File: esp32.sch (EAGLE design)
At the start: 12 parts, among them IC1 LM1117IMPX-3.3, U1 ESP32MOD

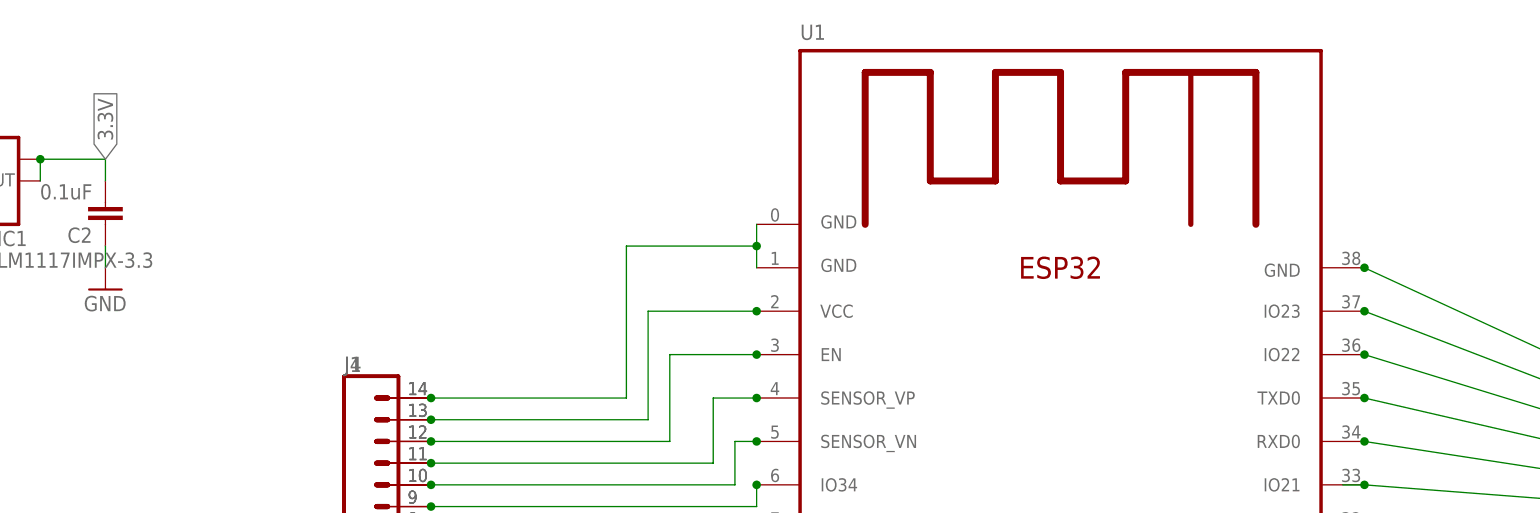
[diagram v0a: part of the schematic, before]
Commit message: Added the reset circuitry
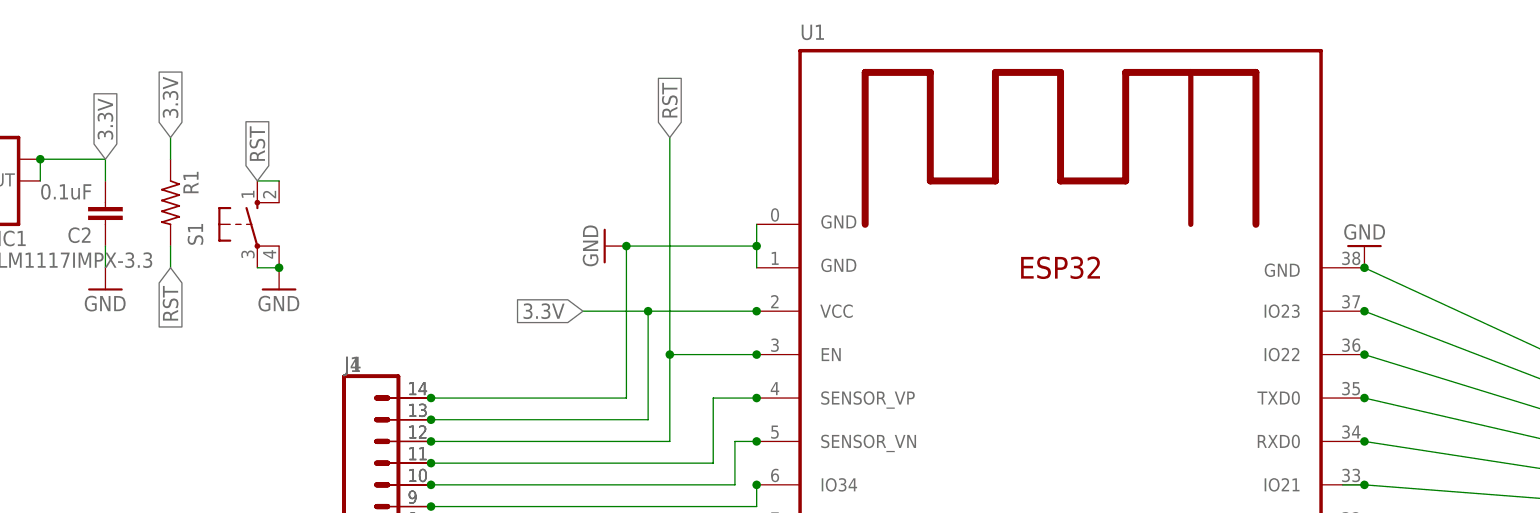
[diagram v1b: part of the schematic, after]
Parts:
- added R1: (no value), rcl:R-US_0411/15
- added S1: (no value), switch-omron:10-XX
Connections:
- removed net N$4: J1.13, J4.13, U1.VCC
- removed net N$5: J1.12, J4.12, U1.EN
- new net RST: J1.12, J4.12, R1.2, S1.S, S1.S1, U1.EN
- net 3.3V: now also J1.13, J4.13, R1.1, U1.VCC
- net GND: now also S1.P, S1.P1
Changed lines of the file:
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@@
 <grid distance="0.1" unitdist="inch" unit="inch" style="lines" multiple="1" display="no" altdistance="0.01" altunitdist="inch" altunit="inch"/>
 <layers>
-<layer number="1" name="Top" color="4" fill="1" visible="no" active="no"/>
-<layer number="16" name="Bottom" color="1" fill="1" visible="no" active="no"/>
-<layer number="17" name="Pads" color="2" fill="1" visible="no" active="no"/>
-<layer number="18" name="Vias" color="2" fill="1" visible="no" active="no"/>
-<layer number="19" name="Unrouted" color="6" fill="1" visible="no" active="no"/>
-<layer number="20" name="Dimension" color="15" fill="1" visible="no" active="no"/>
-<layer number="21" name="tPlace" color="7" fill="1" visible="no" active="no"/>
-<layer number="22" name="bPlace" color="7" fill="1" visible="no" active="no"/>
-<layer number="23" name="tOrigins" color="15" fill="1" visible="no" active="no"/>
-<layer number="24" name="bOrigins" color="15" fill="1" visible="no" active="no"/>
-<layer number="25" name="tNames" color="7" fill="1" visible="no" active="no"/>
-<layer number="26" name="bNames" color="7" fill="1" visible="no" active="no"/>
-<layer number="27" name="tValues" color="7" fill="1" visible="no" active="no"/>
-<layer number="28" name="bValues" color="7" fill="1" visible="no" active="no"/>
+<layer number="1" name="Top" color="4" fill="1" visible="yes" active="no"/>
+<layer number="16" name="Bottom" color="1" fill="1" visible="yes" active="no"/>
+<layer number="17" name="Pads" color="2" fill="1" visible="yes" active="no"/>
+<layer number="18" name="Vias" color="2" fill="1" visible="yes" active="no"/>
+<layer number="19" name="Unrouted" color="6" fill="1" visible="yes" active="no"/>
+<layer number="20" name="Dimension" color="15" fill="1" visible="yes" active="no"/>
+<layer number="21" name="tPlace" color="7" fill="1" visible="yes" active="no"/>
+<layer number="22" name="bPlace" color="7" fill="1" visible="yes" active="no"/>
+<layer number="23" name="tOrigins" color="15" fill="1" visible="yes" active="no"/>
+<layer number="24" name="bOrigins" color="15" fill="1" visible="yes" active="no"/>
+<layer number="25" name="tNames" color="7" fill="1" visible="yes" active="no"/>
+<layer number="26" name="bNames" color="7" fill="1" visible="yes" active="no"/>
+<layer number="27" name="tValues" color="7" fill="1" visible="yes" active="no"/>
+<layer number="28" name="bValues" color="7" fill="1" visible="yes" active="no"/>
 <layer number="29" name="tStop" color="7" fill="3" visible="no" active="no"/>
 <layer number="30" name="bStop" color="7" fill="6" visible="no" active="no"/>
@@
 <layer number="35" name="tGlue" color="7" fill="4" visible="no" active="no"/>
 <layer number="36" name="bGlue" color="7" fill="5" visible="no" active="no"/>
-<layer number="37" name="tTest" color="7" fill="1" visible="no" active="no"/>
-<layer number="38" name="bTest" color="7" fill="1" visible="no" active="no"/>
+<layer number="37" name="tTest" color="7" fill="1" visible="yes" active="no"/>
+<layer number="38" name="bTest" color="7" fill="1" visible="yes" active="no"/>
 <layer number="39" name="tKeepout" color="4" fill="11" visible="no" active="no"/>
 <layer number="40" name="bKeepout" color="1" fill="11" visible="no" active="no"/>
@@
 <layer number="44" name="Drills" color="7" fill="1" visible="no" active="no"/>
 <layer number="45" name="Holes" color="7" fill="1" visible="no" active="no"/>
-<layer number="46" name="Milling" color="3" fill="1" visible="no" active="no"/>
-<layer number="47" name="Measures" color="7" fill="1" visible="no" active="no"/>
-<layer number="48" name="Document" color="7" fill="1" visible="no" active="no"/>
-<layer number="49" name="Reference" color="7" fill="1" visible="no" active="no"/>
-<layer number="50" name="dxf" color="7" fill="1" visible="no" active="no"/>
-<layer number="51" name="tDocu" color="7" fill="1" visible="no" active="no"/>
-<layer number="52" name="bDocu" color="7" fill="1" visible="no" active="no"/>
-<layer number="53" name="tGND_GNDA" color="7" fill="9" visible="no" active="no"/>
-<layer number="54" name="bGND_GNDA" color="1" fill="9" visible="no" active="no"/>
-<layer number="56" name="wert" color="7" fill="1" visible="no" active="no"/>
-<layer number="57" name="tCAD" color="7" fill="1" visible="no" active="no"/>
-<layer number="59" name="tCarbon" color="7" fill="1" visible="no" active="no"/>
-<layer number="60" name="bCarbon" color="7" fill="1" visible="no" active="no"/>
+<layer number="46" name="Milling" color="3" fill="1" visible="yes" active="no"/>
+<layer number="47" name="Measures" color="7" fill="1" visible="yes" active="no"/>
+<layer number="48" name="Document" color="7" fill="1" visible="yes" active="no"/>
+<layer number="49" name="Reference" color="7" fill="1" visible="yes" active="no"/>
+<layer number="50" name="dxf" color="7" fill="1" visible="yes" active="no"/>
+<layer number="51" name="tDocu" color="7" fill="1" visible="yes" active="no"/>
+<layer number="52" name="bDocu" color="7" fill="1" visible="yes" active="no"/>
+<layer number="53" name="tGND_GNDA" color="7" fill="9" visible="yes" active="no"/>
+<layer number="54" name="bGND_GNDA" color="1" fill="9" visible="yes" active="no"/>
+<layer number="56" name="wert" color="7" fill="1" visible="yes" active="no"/>
+<layer number="57" name="tCAD" color="7" fill="1" visible="yes" active="no"/>
+<layer number="59" name="tCarbon" color="7" fill="1" visible="yes" active="no"/>
+<layer number="60" name="bCarbon" color="7" fill="1" visible="yes" active="no"/>
 <layer number="90" name="Modules" color="5" fill="1" visible="yes" active="yes"/>
 <layer number="91" name="Nets" color="2" fill="1" visible="yes" active="yes"/>
@@
 <part name="GND5" library="supply1" deviceset="GND" device=""/>
 <part name="J8" library="SparkFun-Connectors" deviceset="CONN_03" device=""/>
+<part name="R1" library="rcl" deviceset="R-US_" device="0411/15"/>
+<part name="S1" library="switch-omron" deviceset="10-XX" device=""/>
+<part name="GND6" library="supply1" deviceset="GND" device=""/>
+<part name="GND7" library="supply1" deviceset="GND" device=""/>
+<part name="GND8" library="supply1" deviceset="GND" device=""/>
 </parts>
 <sheets>
@@
 <instance part="GND5" gate="1" x="-71.12" y="68.58"/>
 <instance part="J8" gate="J$1" x="-91.44" y="48.26"/>
+<instance part="R1" gate="G$1" x="-38.1" y="78.74" rot="R270"/>
+<instance part="S1" gate="1" x="-27.94" y="76.2"/>
+<instance part="GND6" gate="1" x="-25.4" y="68.58"/>
+<instance part="GND7" gate="1" x="12.7" y="73.66" rot="R270"/>
+<instance part="GND8" gate="1" x="101.6" y="73.66" rot="R180"/>
 </instances>
 <busses>
@@
 <pinref part="J4" gate="G$1" pin="14"/>
 <junction x="-7.62" y="55.88"/>
+<pinref part="GND7" gate="1" pin="GND"/>
+<junction x="15.24" y="73.66"/>
 </segment>
 <segment>
@@
 <pinref part="J5" gate="G$1" pin="1"/>
 <junction x="134.62" y="55.88"/>
+<pinref part="GND8" gate="1" pin="GND"/>
 </segment>
 <segment>
@@
 <label x="-71.12" y="45.72" size="1.778" layer="95" rot="R90" xref="yes"/>
 </segment>
-</net>
-<net name="N$4" class="0">
-<segment>
-<pinref part="J1" gate="G$1" pin="13"/>
-<wire x1="-7.62" y1="53.34" x2="17.78" y2="53.34" width="0.1524" layer="91"/>
-<wire x1="17.78" y1="53.34" x2="17.78" y2="66.04" width="0.1524" layer="91"/>
-<pinref part="U1" gate="G$1" pin="VCC"/>
-<wire x1="17.78" y1="66.04" x2="30.48" y2="66.04" width="0.1524" layer="91"/>
-<junction x="30.48" y="66.04"/>
-<pinref part="J4" gate="G$1" pin="13"/>
-<junction x="-7.62" y="53.34"/>
-</segment>
-</net>
-<net name="N$5" class="0">
+<segment>
+<pinref part="S1" gate="1" pin="P"/>
+<pinref part="S1" gate="1" pin="P1"/>
+<wire x1="-27.94" y1="71.12" x2="-25.4" y2="71.12" width="0.1524" layer="91"/>
+<pinref part="GND6" gate="1" pin="GND"/>
+<junction x="-25.4" y="71.12"/>
+</segment>
+</net>
+<net name="RST" class="0">
 <segment>
 <pinref part="J1" gate="G$1" pin="12"/>
@@
 <pinref part="J4" gate="G$1" pin="12"/>
 <junction x="-7.62" y="50.8"/>
+<label x="20.32" y="86.36" size="1.778" layer="95" rot="R90" xref="yes"/>
+<wire x1="20.32" y1="60.96" x2="20.32" y2="86.36" width="0.1524" layer="91"/>
+<junction x="20.32" y="60.96"/>
+</segment>
+<segment>
+<pinref part="R1" gate="G$1" pin="2"/>
+<wire x1="-38.1" y1="73.66" x2="-38.1" y2="71.12" width="0.1524" layer="91"/>
+<label x="-38.1" y="71.12" size="1.778" layer="95" rot="R270" xref="yes"/>
+</segment>
+<segment>
+<pinref part="S1" gate="1" pin="S"/>
+<pinref part="S1" gate="1" pin="S1"/>
+<wire x1="-27.94" y1="81.28" x2="-25.4" y2="81.28" width="0.1524" layer="91"/>
+<label x="-27.94" y="81.28" size="1.778" layer="95" rot="R90" xref="yes"/>
 </segment>
 </net>
@@
 <label x="-76.2" y="48.26" size="1.778" layer="95" rot="R90" xref="yes"/>
 </segment>
+<segment>
+<pinref part="R1" gate="G$1" pin="1"/>
+<wire x1="-38.1" y1="83.82" x2="-38.1" y2="86.36" width="0.1524" layer="91"/>
+<label x="-38.1" y="86.36" size="1.778" layer="95" rot="R90" xref="yes"/>
+</segment>
+<segment>
+<pinref part="J1" gate="G$1" pin="13"/>
+<wire x1="-7.62" y1="53.34" x2="17.78" y2="53.34" width="0.1524" layer="91"/>
+<wire x1="17.78" y1="53.34" x2="17.78" y2="66.04" width="0.1524" layer="91"/>
+<pinref part="U1" gate="G$1" pin="VCC"/>
+<wire x1="17.78" y1="66.04" x2="30.48" y2="66.04" width="0.1524" layer="91"/>
+<junction x="30.48" y="66.04"/>
+<pinref part="J4" gate="G$1" pin="13"/>
+<junction x="-7.62" y="53.34"/>
+<label x="10.16" y="66.04" size="1.778" layer="95" rot="R180" xref="yes"/>
+<wire x1="10.16" y1="66.04" x2="17.78" y2="66.04" width="0.1524" layer="91"/>
+<junction x="17.78" y="66.04"/>
+</segment>
+</net>
+<net name="GND1" class="0">
 </net>
 </nets>

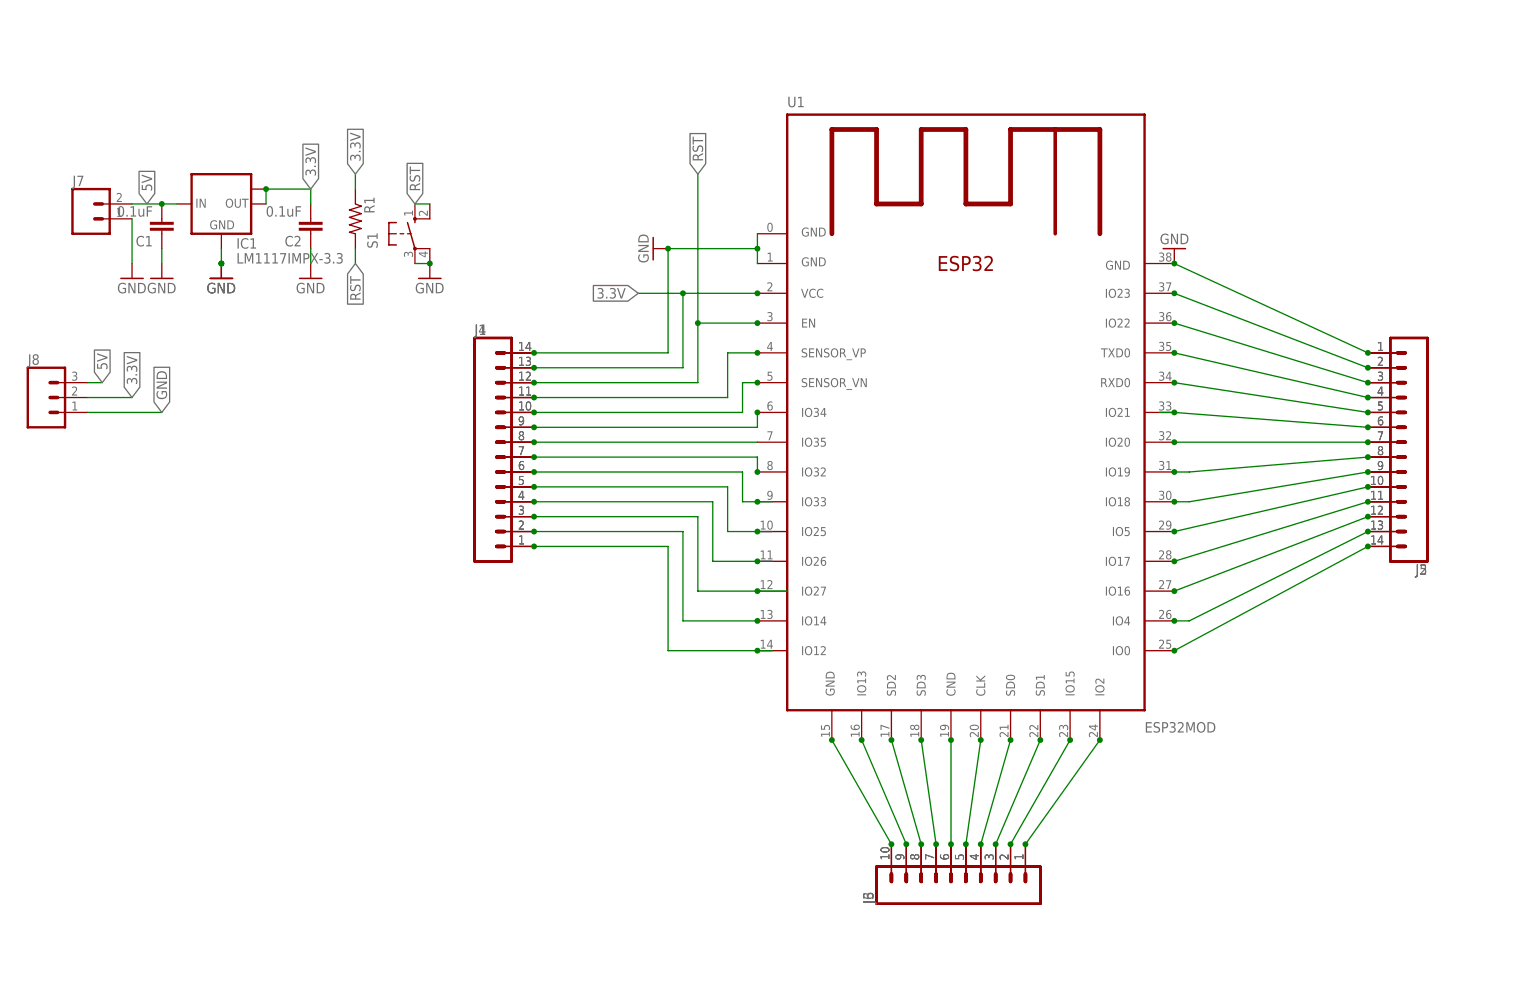
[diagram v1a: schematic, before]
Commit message: Added all the GPIO strapping bias resistors
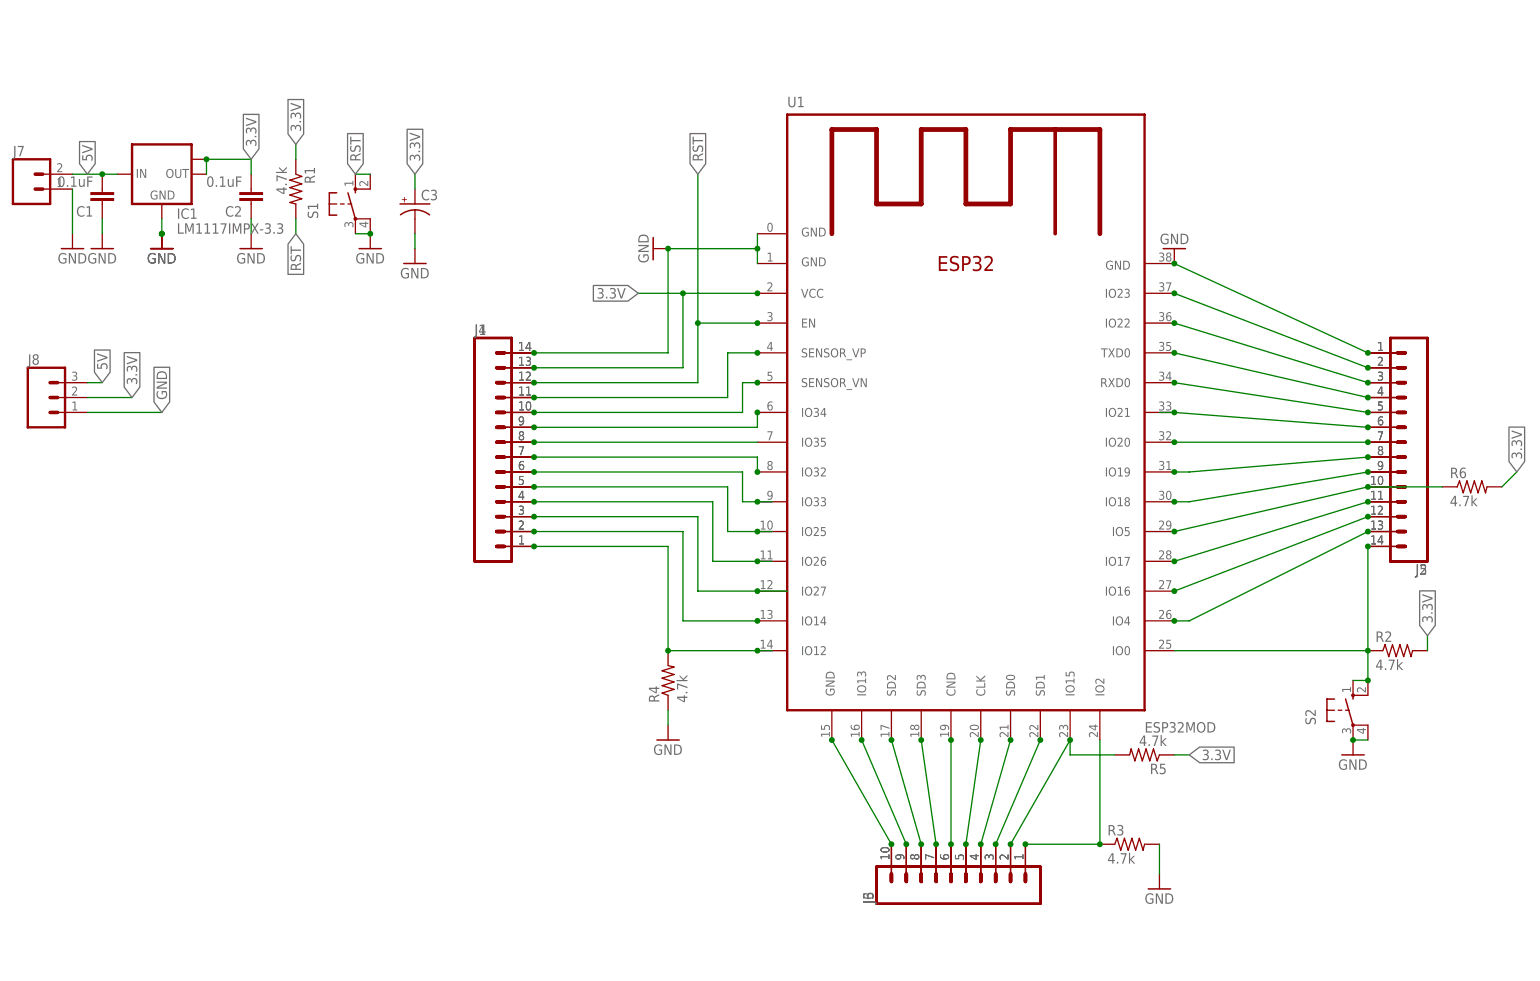
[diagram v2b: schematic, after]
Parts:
- added C3: (no value), rcl:CPOL-USE3.5-8
- added R2, R3, R4, R5, R6: 4.7k, rcl:R-US_0411/15
- added S2: (no value), switch-omron:10-XX
- R1: value (none) -> 4.7k
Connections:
- net 3.3V: now also C3.+, R2.2, R5.1, R6.2
- net GND: now also C3.-, R3.2, R4.1, S2.P, S2.P1
- net N$14: now also R4.2
- net N$19: now also R6.1
- net N$28: now also R2.1, S2.S, S2.S1
- net N$37: now also R5.2
- net N$38: now also R3.1
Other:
- moved on the sheet: C1, C2, IC1, J7, R1, S1
